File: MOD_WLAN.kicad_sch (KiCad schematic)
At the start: 1 part, among them U6 ESP32-C3-WROOM-02

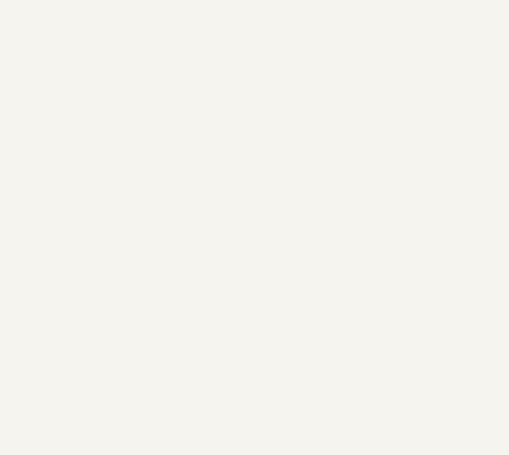
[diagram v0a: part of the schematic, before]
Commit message: routed more sheets, improved analogs. next 5v /analog ground
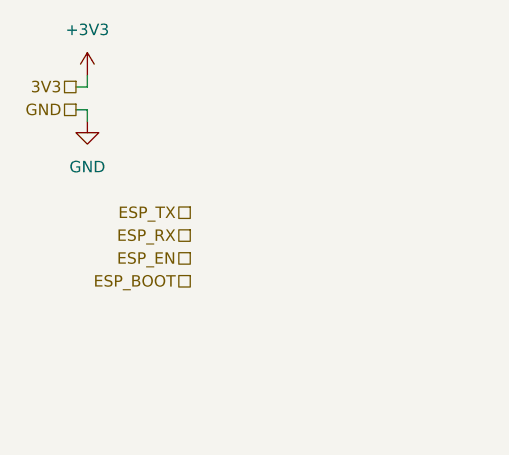
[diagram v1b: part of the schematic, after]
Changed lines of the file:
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@@
 	(generator_version "9.0")
 	(paper "A4")
+	(wire
+		(pts
+			(xy 25.4 25.4) (xy 26.67 25.4)
+		)
+		(stroke
+			(width 0)
+			(type default)
+		)
+	)
+	(wire
+		(pts
+			(xy 25.4 27.94) (xy 26.67 27.94)
+		)
+		(stroke
+			(width 0)
+			(type default)
+		)
+	)
+	(wire
+		(pts
+			(xy 26.67 25.4) (xy 26.67 24.13)
+		)
+		(stroke
+			(width 0)
+			(type default)
+		)
+	)
+	(wire
+		(pts
+			(xy 26.67 27.94) (xy 26.67 29.21)
+		)
+		(stroke
+			(width 0)
+			(type default)
+		)
+	)
+	(hierarchical_label "ESP_BOOT"
+		(shape passive)
+		(at 38.1 46.99 180)
+		(effects
+			(font
+				(size 1.27 1.27)
+			)
+			(justify right)
+		)
+	)
+	(hierarchical_label "ESP_EN"
+		(shape passive)
+		(at 38.1 44.45 180)
+		(effects
+			(font
+				(size 1.27 1.27)
+			)
+			(justify right)
+		)
+	)
+	(hierarchical_label "ESP_RX"
+		(shape passive)
+		(at 38.1 41.91 180)
+		(effects
+			(font
+				(size 1.27 1.27)
+			)
+			(justify right)
+		)
+	)
+	(hierarchical_label "GND"
+		(shape passive)
+		(at 25.4 27.94 180)
+		(effects
+			(font
+				(size 1.27 1.27)
+			)
+			(justify right)
+		)
+	)
+	(hierarchical_label "3V3"
+		(shape passive)
+		(at 25.4 25.4 180)
+		(effects
+			(font
+				(size 1.27 1.27)
+			)
+			(justify right)
+		)
+	)
+	(hierarchical_label "ESP_TX"
+		(shape passive)
+		(at 38.1 39.37 180)
+		(effects
+			(font
+				(size 1.27 1.27)
+			)
+			(justify right)
+		)
+	)
+	(symbol
+		(lib_id "power:+3V3")
+		(at 26.67 24.13 0)
+		(unit 1)
+		(exclude_from_sim no)
+		(in_bom yes)
+		(on_board yes)
+		(dnp no)
+		(fields_autoplaced yes)
+		(property "Reference" "#PWR0130"
+			(at 26.67 27.94 0)
+			(effects
+				(font
+					(size 1.27 1.27)
+				)
+				(hide yes)
+			)
+		)
+		(property "Value" "+3V3"
+			(at 26.67 19.05 0)
+			(effects
+				(font
+					(size 1.27 1.27)
+				)
+			)
+		)
+		(property "Footprint" ""
+			(at 26.67 24.13 0)
+			(effects
+				(font
+					(size 1.27 1.27)
+				)
+				(hide yes)
+			)
+		)
+		(property "Datasheet" ""
+			(at 26.67 24.13 0)
+			(effects
+				(font
+					(size 1.27 1.27)
+				)
+				(hide yes)
+			)
+		)
+		(property "Description" "Power symbol creates a global label with name \"+3V3\""
+			(at 26.67 24.13 0)
+			(effects
+				(font
+					(size 1.27 1.27)
+				)
+				(hide yes)
+			)
+		)
+		(pin "1"
+		)
+		(instances
+			(project "NCU"
+				(path "/3aee14c3-5480-4f7c-989e-3fef81779034/0cdbc80d-6682-4488-acea-b93c92a9f88d"
+					(reference "#PWR0130")
+					(unit 1)
+				)
+			)
+		)
+	)
 	(symbol
 		(lib_id "RF_Module:ESP32-C3-WROOM-02")
@@
 					(unit 1)
 				)
+			)
+		)
+	)
+	(symbol
+		(lib_id "power:GND")
+		(at 26.67 29.21 0)
+		(unit 1)
+		(exclude_from_sim no)
+		(in_bom yes)
+		(on_board yes)
+		(dnp no)
+		(fields_autoplaced yes)
+		(property "Reference" "#PWR0131"
+			(at 26.67 35.56 0)
+			(effects
+				(font
+					(size 1.27 1.27)
+				)
+				(hide yes)
+			)
+		)
+		(property "Value" "GND"
+			(at 26.67 34.29 0)
+			(effects
+				(font
+					(size 1.27 1.27)
+				)
+			)
+		)
+		(property "Footprint" ""
+			(at 26.67 29.21 0)
+			(effects
+				(font
+					(size 1.27 1.27)
+				)
+				(hide yes)
+			)
+		)
+		(property "Datasheet" ""
+			(at 26.67 29.21 0)
+			(effects
+				(font
+					(size 1.27 1.27)
+				)
+				(hide yes)
+			)
+		)
+		(property "Description" "Power symbol creates a global label with name \"GND\" , ground"
+			(at 26.67 29.21 0)
+			(effects
+				(font
+					(size 1.27 1.27)
+				)
+				(hide yes)
+			)
+		)
+		(pin "1"
+		)
+		(instances
+			(project "NCU"
+				(path "/3aee14c3-5480-4f7c-989e-3fef81779034/0cdbc80d-6682-4488-acea-b93c92a9f88d"
+					(reference "#PWR0131")
+					(unit 1)
+				)

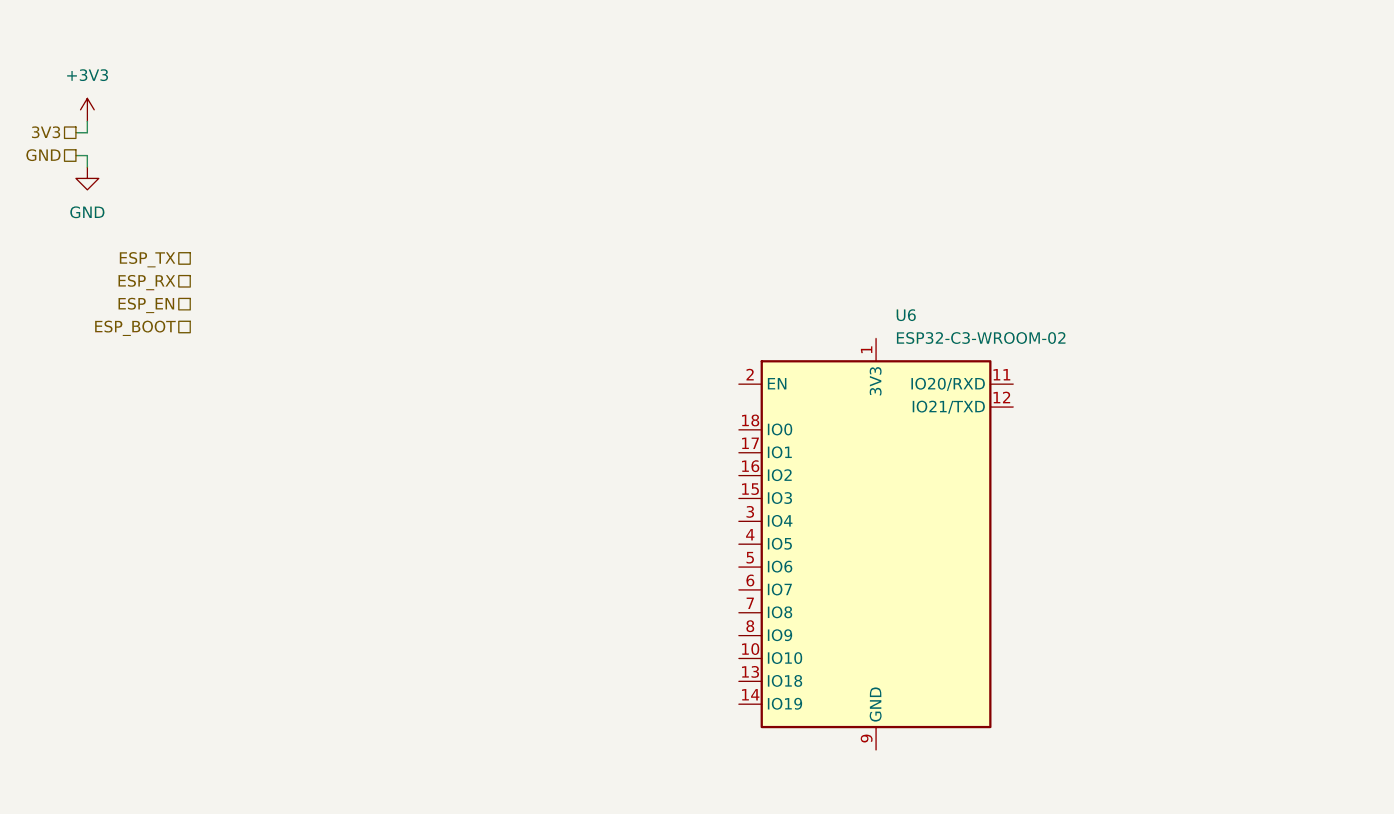
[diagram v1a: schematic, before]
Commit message: finished initial esp routing
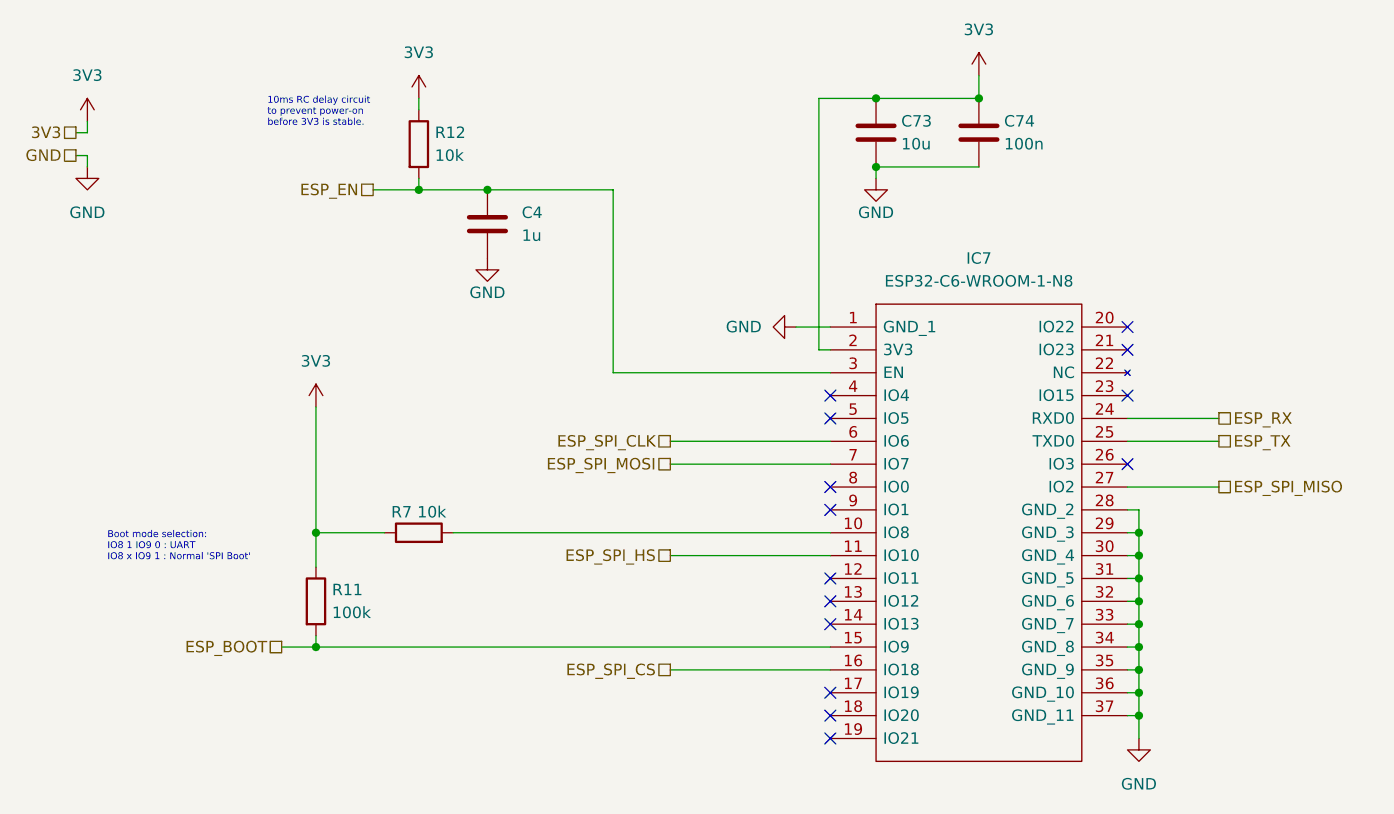
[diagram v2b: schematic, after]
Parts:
- removed U6: ESP32-C3-WROOM-02, RF_Module:ESP32-C3-WROOM-02, symbol RF_Module:ESP32-C3-WROOM-02
- added C4: 1u, Capacitor_SMD:C_0603_1608Metric_Pad1.08x0.95mm_HandSolder, symbol Device:C
- added C73: 10u, Capacitor_SMD:C_0603_1608Metric_Pad1.08x0.95mm_HandSolder, symbol Device:C
- added C74: 100n, Capacitor_SMD:C_0603_1608Metric_Pad1.08x0.95mm_HandSolder, symbol Device:C
- added IC7: ESP32-C6-WROOM-1-N8, ESP32C6WROOM1N8, symbol 0_SamacSys_Parts:ESP32-C6-WROOM-1-N8
- added R11: 100k, Resistor_SMD:R_0603_1608Metric_Pad0.98x0.95mm_HandSolder, symbol Device:R
- added R12, R7: 10k, Resistor_SMD:R_0603_1608Metric_Pad0.98x0.95mm_HandSolder, symbol Device:R
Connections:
- net ESP_BOOT: now also IC7.15 (IO9), R11.2
- net ESP_EN: now also C4.1, IC7.3 (EN), R12.2
- net ESP_RX: now also IC7.24 (RXD0)
- net ESP_TX: now also IC7.25 (TXD0)
- net GND: now also C4.2, C73.2, C74.2, IC7.1 (GND_1), IC7.28 (GND_2), IC7.29 (GND_3), IC7.30 (GND_4), IC7.31 (GND_5), IC7.32 (GND_6), IC7.33 (GND_7), IC7.34 (GND_8), IC7.35 (GND_9), IC7.36 (GND_10), IC7.37 (GND_11)
- new net: IC7.10 (IO8), R7.2
- new net 3V3: C73.1, C74.1, IC7.2 (3V3), R11.1, R12.1, R7.1
- new net ESP_SPI_CLK: IC7.6 (IO6)
- new net ESP_SPI_CS: IC7.16 (IO18)
- new net ESP_SPI_HS: IC7.11 (IO10)
- new net ESP_SPI_MISO: IC7.27 (IO2)
- new net ESP_SPI_MOSI: IC7.7 (IO7)
- no-connect marks 0 -> 14

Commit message: added dip switches to wireless disables
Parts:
- added SW2: SW_DIP_x01, symbol Switch:SW_DIP_x01
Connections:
- net ESP_EN: now also SW2.1
- net GND: now also SW2.2
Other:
- moved on the sheet: C4
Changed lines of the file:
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@@
-	)
-	(junction
-		(at 71.12 31.75)
-		(diameter 0)
-		(color 0 0 0 0)
 	)
 	(junction
@@
 	)
 	(junction
+		(at 92.71 40.64)
+		(diameter 0)
+		(color 0 0 0 0)
+	)
+	(junction
 		(at 143.51 69.85)
 		(diameter 0)
@@
 	)
 	(junction
+		(at 67.31 40.64)
+		(diameter 0)
+		(color 0 0 0 0)
+	)
+	(junction
+		(at 67.31 31.75)
+		(diameter 0)
+		(color 0 0 0 0)
+	)
+	(junction
 		(at 52.07 82.55)
 		(diameter 0)
@@
 	(wire
 		(pts
-			(xy 71.12 31.75) (xy 63.5 31.75)
+			(xy 67.31 40.64) (xy 76.2 40.64)
 		)
 		(stroke
@@
 	(wire
 		(pts
+			(xy 92.71 40.64) (xy 91.44 40.64)
+		)
+		(stroke
+			(width 0)
+			(type default)
+		)
+	)
+	(wire
+		(pts
 			(xy 143.51 72.39) (xy 142.24 72.39)
 		)
@@
 	(wire
 		(pts
-			(xy 71.12 31.75) (xy 85.09 31.75)
-		)
-		(stroke
-			(width 0)
-			(type default)
-		)
-	)
-	(wire
-		(pts
 			(xy 142.24 80.01) (xy 143.51 80.01)
 		)
@@
 	(wire
 		(pts
+			(xy 67.31 40.64) (xy 67.31 43.18)
+		)
+		(stroke
+			(width 0)
+			(type default)
+		)
+	)
+	(wire
+		(pts
 			(xy 142.24 57.15) (xy 152.4 57.15)
 		)
@@
 	(wire
 		(pts
-			(xy 85.09 52.07) (xy 109.22 52.07)
+			(xy 92.71 52.07) (xy 109.22 52.07)
 		)
 		(stroke
@@
 	(wire
 		(pts
+			(xy 92.71 31.75) (xy 92.71 40.64)
+		)
+		(stroke
+			(width 0)
+			(type default)
+		)
+	)
+	(wire
+		(pts
 			(xy 142.24 85.09) (xy 143.51 85.09)
 		)
@@
 	(wire
 		(pts
-			(xy 85.09 31.75) (xy 85.09 52.07)
-		)
-		(stroke
-			(width 0)
-			(type default)
-		)
-	)
-	(wire
-		(pts
 			(xy 143.51 77.47) (xy 143.51 74.93)
 		)
@@
 	(wire
 		(pts
+			(xy 67.31 31.75) (xy 63.5 31.75)
+		)
+		(stroke
+			(width 0)
+			(type default)
+		)
+	)
+	(wire
+		(pts
+			(xy 67.31 40.64) (xy 67.31 39.37)
+		)
+		(stroke
+			(width 0)
+			(type default)
+		)
+	)
+	(wire
+		(pts
 			(xy 143.51 67.31) (xy 142.24 67.31)
 		)
@@
 	(wire
 		(pts
+			(xy 92.71 40.64) (xy 92.71 52.07)
+		)
+		(stroke
+			(width 0)
+			(type default)
+		)
+	)
+	(wire
+		(pts
 			(xy 107.95 21.59) (xy 114.3 21.59)
 		)
@@
 	(wire
 		(pts
+			(xy 67.31 31.75) (xy 92.71 31.75)
+		)
+		(stroke
+			(width 0)
+			(type default)
+		)
+	)
+	(wire
+		(pts
+			(xy 50.8 31.75) (xy 63.5 31.75)
+		)
+		(stroke
+			(width 0)
+			(type default)
+		)
+	)
+	(wire
+		(pts
 			(xy 26.67 27.94) (xy 26.67 29.21)
 		)
@@
 		(pts
 			(xy 52.07 55.88) (xy 52.07 69.85)
-		)
-		(stroke
-			(width 0)
-			(type default)
-		)
-	)
-	(wire
-		(pts
-			(xy 58.42 31.75) (xy 63.5 31.75)
 		)
 		(stroke
@@
 	(hierarchical_label "ESP_EN"
 		(shape passive)
-		(at 58.42 31.75 180)
+		(at 50.8 31.75 180)
 		(effects
 			(font
@@
 				(path "/3aee14c3-5480-4f7c-989e-3fef81779034/0cdbc80d-6682-4488-acea-b93c92a9f88d"
 					(reference "#PWR0306")
+					(unit 1)
+				)
+			)
+		)
+	)
+	(symbol
+		(lib_id "Switch:SW_DIP_x01")
+		(at 83.82 40.64 0)
+		(mirror y)
+		(unit 1)
+		(exclude_from_sim no)
+		(in_bom yes)
+		(on_board yes)
+		(dnp no)
+		(property "Reference" "SW2"
+			(at 75.692 36.322 0)
+			(effects
+				(font
+					(size 1.27 1.27)
+				)
+				(justify right)
+			)
+		)
+		(property "Value" "SW_DIP_x01"
+			(at 80.772 36.068 0)
+			(effects
+				(font
+					(size 1.27 1.27)
+				)
+				(justify right)
+			)
+		)
+		(property "Footprint" ""
+			(at 83.82 40.64 0)
+			(effects
+				(font
+					(size 1.27 1.27)
+				)
+				(hide yes)
+			)
+		)
+		(property "Datasheet" "~"
+			(at 83.82 40.64 0)
+			(effects
+				(font
+					(size 1.27 1.27)
+				)
+				(hide yes)
+			)
+		)
+		(property "Description" "1x DIP Switch, Single Pole Single Throw (SPST) switch, small symbol"
+			(at 83.82 40.64 0)
+			(effects
+				(font
+					(size 1.27 1.27)
+				)
+				(hide yes)
+			)
+		)
+		(pin "2"
+		)
+		(pin "1"
+		)
+		(instances
+			(project "NCU"
+				(path "/3aee14c3-5480-4f7c-989e-3fef81779034/0cdbc80d-6682-4488-acea-b93c92a9f88d"
+					(reference "SW2")
 					(unit 1)
 				)
@@
 	(symbol
 		(lib_id "Device:C")
-		(at 71.12 35.56 0)
+		(at 67.31 35.56 0)
 		(unit 1)
 		(exclude_from_sim no)
@@
 		(on_board yes)
 		(dnp no)
-		(fields_autoplaced yes)
 		(property "Reference" "C4"
-			(at 74.93 34.2899 0)
+			(at 71.12 34.2899 0)
 			(effects
 				(font
@@
 		)
 		(property "Value" "1u"
-			(at 74.93 36.8299 0)
+			(at 71.374 36.576 0)
 			(effects
 				(font
@@
 		)
 		(property "Footprint" "Capacitor_SMD:C_0603_1608Metric_Pad1.08x0.95mm_HandSolder"
-			(at 72.0852 39.37 0)
+			(at 68.2752 39.37 0)
 			(effects
 				(font
@@
 		)
 		(property "Datasheet" "~"
-			(at 71.12 35.56 0)
+			(at 67.31 35.56 0)
 			(effects
 				(font
@@
 		)
 		(property "Description" "Unpolarized capacitor"
-			(at 71.12 35.56 0)
+			(at 67.31 35.56 0)
 			(effects
 				(font
@@
 	(symbol
 		(lib_id "power:GND")
-		(at 71.12 39.37 0)
+		(at 67.31 43.18 0)
 		(unit 1)
 		(exclude_from_sim no)
@@
 		(dnp no)
 		(property "Reference" "#PWR0304"
-			(at 71.12 45.72 0)
+			(at 67.31 49.53 0)
 			(effects
 				(font
@@
 		)
 		(property "Value" "GND"
-			(at 71.12 43.18 0)
+			(at 67.31 46.99 0)
 			(effects
 				(font
@@
 		)
 		(property "Footprint" ""
-			(at 71.12 39.37 0)
+			(at 67.31 43.18 0)
 			(effects
 				(font
@@
 		)
 		(property "Datasheet" ""
-			(at 71.12 39.37 0)
+			(at 67.31 43.18 0)
 			(effects
 				(font
@@
 		)
 		(property "Description" "Power symbol creates a global label with name \"GND\" , ground"
-			(at 71.12 39.37 0)
-			(effects
-				(font
+			(at 67.31 43.18 0)
+			(effects
+				(font

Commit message: initial full port selection
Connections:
- net ESP_SPI_HS: no longer names the net of IC7.11 (IO10)
- no-connect marks 14 -> 15
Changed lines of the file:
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@@
+	)
+	(no_connect
+		(at 109.22 92.71)
+	)
+	(no_connect
+		(at 109.22 90.17)
+	)
+	(no_connect
+		(at 109.22 57.15)
+	)
+	(no_connect
+		(at 109.22 72.39)
 	)
 	(no_connect
@@
 	)
 	(no_connect
-		(at 109.22 92.71)
-	)
-	(no_connect
-		(at 109.22 90.17)
-	)
-	(no_connect
-		(at 109.22 57.15)
-	)
-	(no_connect
 		(at 142.24 49.53)
 	)
@@
 	(wire
 		(pts
-			(xy 91.44 72.39) (xy 109.22 72.39)
-		)
-		(stroke
-			(width 0)
-			(type default)
-		)
-	)
-	(wire
-		(pts
 			(xy 114.3 29.21) (xy 125.73 29.21)
 		)
@@
 		)
 	)
-	(hierarchical_label "ESP_SPI_HS"
-		(shape passive)
-		(at 91.44 72.39 180)
-		(effects
-			(font
-				(size 1.27 1.27)
-			)
-			(justify right)
-		)
-	)
